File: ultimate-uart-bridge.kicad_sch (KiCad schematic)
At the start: 22 parts, among them J101 Conn_02x03_Row_Letter_First

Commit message: New inital routing
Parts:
- C101, C102: value (none) -> 1uF; footprint (none) -> Capacitor_SMD:C_0805_2012Metric_Pad1.18x1.45mm_HandSolder
- C103, C104: value (none) -> 47pF; footprint (none) -> Capacitor_SMD:C_0805_2012Metric_Pad1.18x1.45mm_HandSolder
- C105, C107: value (none) -> 100nF; footprint (none) -> Capacitor_SMD:C_0805_2012Metric_Pad1.18x1.45mm_HandSolder
- C106: value (none) -> 10nF; footprint (none) -> Capacitor_SMD:C_0805_2012Metric_Pad1.18x1.45mm_HandSolder
- C108: value (none) -> 4.7uF; footprint (none) -> Capacitor_SMD:C_0805_2012Metric_Pad1.18x1.45mm_HandSolder
- D101, D102: value (none) -> LED; footprint (none) -> LED_SMD:LED_0805_2012Metric_Pad1.15x1.40mm_HandSolder
- FB101: value (none) -> Ferrite_Bead_Small; footprint (none) -> Inductor_SMD:L_0805_2012Metric_Pad1.15x1.40mm_HandSolder
- I101: value (none) -> MIC5317-1.8YM5-TR
- I102: value (none) -> FT231XS; footprint (none) -> Package_SO:SSOP-20_3.9x8.7mm_P0.635mm
- J101: footprint (none) -> Connector_PinHeader_2.54mm:PinHeader_2x03_P2.54mm_Vertical_SMD; symbol Connector_Generic:Conn_02x03_Row_Letter_First -> Connector_Generic:Conn_02x03_Odd_Even
- J102: value (none) -> USB_C_Receptacle_USB2.0; footprint (none) -> Connector_USB:USB_C_Receptacle_GCT_USB4085
- J103: value (none) -> Conn_01x03; footprint (none) -> Connector_PinHeader_2.54mm:PinHeader_1x03_P2.54mm_Vertical_SMD_Pin1Left
- R101, R102: value (none) -> 27; footprint (none) -> Resistor_SMD:R_0805_2012Metric_Pad1.20x1.40mm_HandSolder
- R103, R104: value (none) -> R; footprint (none) -> Resistor_SMD:R_0805_2012Metric_Pad1.20x1.40mm_HandSolder
- R105, R106: value (none) -> 5.1k; footprint (none) -> Resistor_SMD:R_0805_2012Metric_Pad1.20x1.40mm_HandSolder
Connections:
- net +1V8: now also J101.6 (Pin_6); no longer J101.b3 (Pin_b3)
- net +3V3: now also J101.4 (Pin_4); no longer J101.b2 (Pin_b2)
- net VBUS: now also J101.2 (Pin_2); no longer J101.b1 (Pin_b1)
- net VCCIO: now also J101.1 (Pin_1), J101.3 (Pin_3), J101.5 (Pin_5); no longer J101.a1 (Pin_a1), J101.a2 (Pin_a2), J101.a3 (Pin_a3)

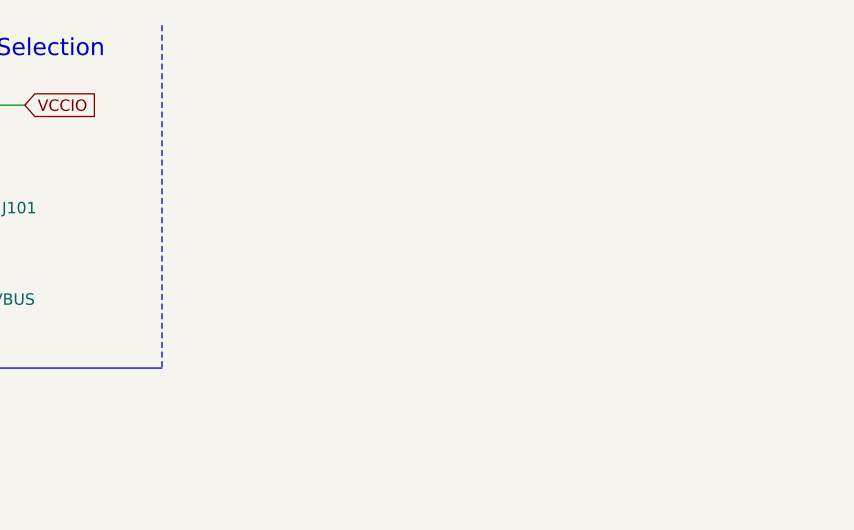
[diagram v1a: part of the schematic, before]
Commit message: Add testpoints and text
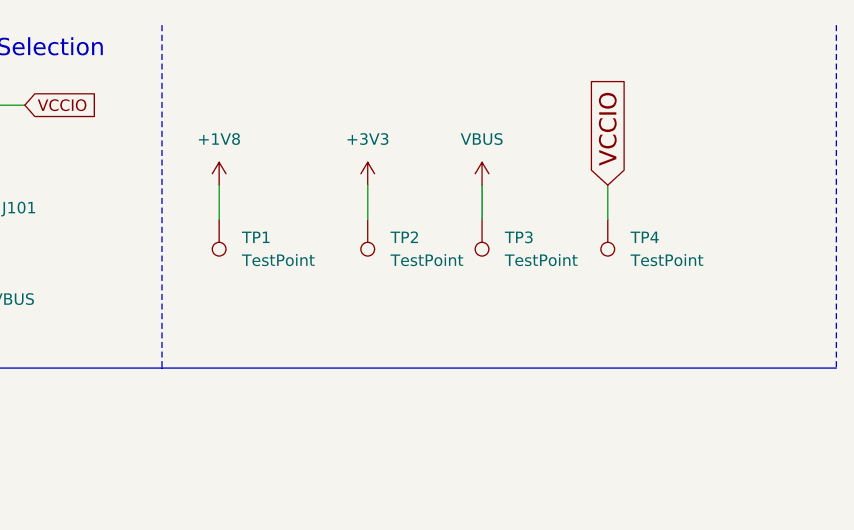
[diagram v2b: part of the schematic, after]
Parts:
- added TP1, TP2, TP3, TP4: TestPoint, TestPoint:TestPoint_Pad_D3.0mm, symbol Connector:TestPoint
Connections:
- net +1V8: now also TP1.1
- net +3V3: now also TP2.1
- net VBUS: now also TP3.1
- net VCCIO: now also TP4.1
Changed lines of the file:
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@@
+    (stroke (width 0) (type default) (color 0 0 0 0))
+  )
+  (wire (pts (xy 179.07 30.48) (xy 179.07 34.29))
     (stroke (width 0) (type default) (color 0 0 0 0))
   )
@@
     (stroke (width 0) (type default) (color 0 0 0 0))
   )
+  (wire (pts (xy 208.28 30.48) (xy 208.28 34.29))
+    (stroke (width 0) (type default) (color 0 0 0 0))
+  )
   (wire (pts (xy 109.22 90.17) (xy 119.38 90.17))
     (stroke (width 0) (type default) (color 0 0 0 0))
@@
   )
   (wire (pts (xy 54.61 83.82) (xy 50.8 83.82))
+    (stroke (width 0) (type default) (color 0 0 0 0))
+  )
+  (wire (pts (xy 222.25 30.48) (xy 222.25 34.29))
     (stroke (width 0) (type default) (color 0 0 0 0))
   )
@@
     (stroke (width 0) (type default) (color 0 0 0 0))
   )
+  (polyline (pts (xy 172.72 50.8) (xy 247.65 50.8))
+    (stroke (width 0) (type default) (color 0 0 0 1))
+  )
   (wire (pts (xy 34.29 29.21) (xy 41.91 29.21))
+    (stroke (width 0) (type default) (color 0 0 0 0))
+  )
+  (wire (pts (xy 195.58 30.48) (xy 195.58 34.29))
     (stroke (width 0) (type default) (color 0 0 0 0))
   )
@@
   (wire (pts (xy 50.8 81.28) (xy 54.61 81.28))
     (stroke (width 0) (type default) (color 0 0 0 0))
+  )
+  (polyline (pts (xy 247.65 12.7) (xy 247.65 50.8))
+    (stroke (width 0) (type dash) (color 0 0 0 1))
   )
   (wire (pts (xy 54.61 81.28) (xy 54.61 83.82))
@@
     (property "Intersheet References" "${INTERSHEET_REFS}" (id 0) (at 0 0 0)
       (effects (font (size 1.27 1.27)) hide)
+    )
+  )
+  (global_label "VCCIO" (shape input) (at 222.25 30.48 90) (fields_autoplaced)
+    (effects (font (size 1.905 1.905)) (justify left))
+    (property "Intersheet References" "${INTERSHEET_REFS}" (id 0) (at 222.131 18.6482 90)
+      (effects (font (size 1.905 1.905)) (justify left) hide)
     )
   )
@@
     (pin "1")
   )
+  (symbol (lib_id "Connector:TestPoint") (at 195.58 34.29 180) (unit 1)
+    (in_bom yes) (on_board yes) (fields_autoplaced)
+    (property "Reference" "TP2" (id 0) (at 198.12 36.3219 0)
+      (effects (font (size 1.27 1.27)) (justify right))
+    )
+    (property "Value" "TestPoint" (id 1) (at 198.12 38.8619 0)
+      (effects (font (size 1.27 1.27)) (justify right))
+    )
+    (property "Footprint" "TestPoint:TestPoint_Pad_D3.0mm" (id 2) (at 190.5 34.29 0)
+      (effects (font (size 1.27 1.27)) hide)
+    )
+    (property "Datasheet" "~" (id 3) (at 190.5 34.29 0)
+      (effects (font (size 1.27 1.27)) hide)
+    )
+    (pin "1")
+  )
+  (symbol (lib_id "power:VBUS") (at 208.28 30.48 0) (unit 1)
+    (in_bom yes) (on_board yes) (fields_autoplaced)
+    (property "Reference" "#PWR03" (id 0) (at 208.28 34.29 0)
+      (effects (font (size 1.27 1.27)) hide)
+    )
+    (property "Value" "VBUS" (id 1) (at 208.28 25.4 0))
+    (property "Footprint" "" (id 2) (at 208.28 30.48 0)
+      (effects (font (size 1.27 1.27)) hide)
+    )
+    (property "Datasheet" "" (id 3) (at 208.28 30.48 0)
+      (effects (font (size 1.27 1.27)) hide)
+    )
+    (pin "1")
+  )
+  (symbol (lib_id "Connector:TestPoint") (at 208.28 34.29 180) (unit 1)
+    (in_bom yes) (on_board yes) (fields_autoplaced)
+    (property "Reference" "TP3" (id 0) (at 210.82 36.3219 0)
+      (effects (font (size 1.27 1.27)) (justify right))
+    )
+    (property "Value" "TestPoint" (id 1) (at 210.82 38.8619 0)
+      (effects (font (size 1.27 1.27)) (justify right))
+    )
+    (property "Footprint" "TestPoint:TestPoint_Pad_D3.0mm" (id 2) (at 203.2 34.29 0)
+      (effects (font (size 1.27 1.27)) hide)
+    )
+    (property "Datasheet" "~" (id 3) (at 203.2 34.29 0)
+      (effects (font (size 1.27 1.27)) hide)
+    )
+    (pin "1")
+  )
+  (symbol (lib_id "power:+3V3") (at 195.58 30.48 0) (unit 1)
+    (in_bom yes) (on_board yes) (fields_autoplaced)
+    (property "Reference" "#PWR02" (id 0) (at 195.58 34.29 0)
+      (effects (font (size 1.27 1.27)) hide)
+    )
+    (property "Value" "+3V3" (id 1) (at 195.58 25.4 0))
+    (property "Footprint" "" (id 2) (at 195.58 30.48 0)
+      (effects (font (size 1.27 1.27)) hide)
+    )
+    (property "Datasheet" "" (id 3) (at 195.58 30.48 0)
+      (effects (font (size 1.27 1.27)) hide)
+    )
+    (pin "1")
+  )
+  (symbol (lib_id "Connector:TestPoint") (at 179.07 34.29 180) (unit 1)
+    (in_bom yes) (on_board yes) (fields_autoplaced)
+    (property "Reference" "TP1" (id 0) (at 181.61 36.3219 0)
+      (effects (font (size 1.27 1.27)) (justify right))
+    )
+    (property "Value" "TestPoint" (id 1) (at 181.61 38.8619 0)
+      (effects (font (size 1.27 1.27)) (justify right))
+    )
+    (property "Footprint" "TestPoint:TestPoint_Pad_D3.0mm" (id 2) (at 173.99 34.29 0)
+      (effects (font (size 1.27 1.27)) hide)
+    )
+    (property "Datasheet" "~" (id 3) (at 173.99 34.29 0)
+      (effects (font (size 1.27 1.27)) hide)
+    )
+    (pin "1")
+  )
+  (symbol (lib_id "Connector:TestPoint") (at 222.25 34.29 180) (unit 1)
+    (in_bom yes) (on_board yes) (fields_autoplaced)
+    (property "Reference" "TP4" (id 0) (at 224.79 36.3219 0)
+      (effects (font (size 1.27 1.27)) (justify right))
+    )
+    (property "Value" "TestPoint" (id 1) (at 224.79 38.8619 0)
+      (effects (font (size 1.27 1.27)) (justify right))
+    )
+    (property "Footprint" "TestPoint:TestPoint_Pad_D3.0mm" (id 2) (at 217.17 34.29 0)
+      (effects (font (size 1.27 1.27)) hide)
+    )
+    (property "Datasheet" "~" (id 3) (at 217.17 34.29 0)
+      (effects (font (size 1.27 1.27)) hide)
+    )
+    (pin "1")
+  )
+  (symbol (lib_id "power:+1V8") (at 179.07 30.48 0) (unit 1)
+    (in_bom yes) (on_board yes) (fields_autoplaced)
+    (property "Reference" "#PWR01" (id 0) (at 179.07 34.29 0)
+      (effects (font (size 1.27 1.27)) hide)
+    )
+    (property "Value" "+1V8" (id 1) (at 179.07 25.4 0))
+    (property "Footprint" "" (id 2) (at 179.07 30.48 0)
+      (effects (font (size 1.27 1.27)) hide)
+    )
+    (property "Datasheet" "" (id 3) (at 179.07 30.48 0)
+      (effects (font (size 1.27 1.27)) hide)
+    )
+    (pin "1")
+  )
   (sheet_instances
     (path "/" (page "1"))
   )
   (symbol_instances
+    (path "/d447cd8d-505f-45cd-b508-7b48bbd46143"
+      (reference "#PWR01") (unit 1) (value "+1V8") (footprint "")
+    )
+    (path "/918c1faf-a3b6-4f0c-9710-820ea771bcfb"
+      (reference "#PWR02") (unit 1) (value "+3V3") (footprint "")
+    )
+    (path "/51ff3703-38a9-4abd-b6b0-2e764a7ec977"
+      (reference "#PWR03") (unit 1) (value "VBUS") (footprint "")
+    )
     (path "/00000000-0000-0000-0000-000060fe5cbe"
       (reference "#PWR0101") (unit 1) (value "VBUS") (footprint "")
@@
       (reference "R106") (unit 1) (value "5.1k") (footprint "Resistor_SMD:R_0805_2012Metric_Pad1.20x1.40mm_HandSolder")
     )
-  )
+    (path "/b6ba5c02-0398-48b3-9194-4c168c5cb2de"
+      (reference "TP1") (unit 1) (value "TestPoint") (footprint "TestPoint:TestPoint_Pad_D3.0mm")
+    )
+    (path "/1011f139-ec9e-4d31-a10a-d23eea101c42"
+      (reference "TP2") (unit 1) (value "TestPoint") (footprint "TestPoint:TestPoint_Pad_D3.0mm")
+    )
+    (path "/6f46363d-2716-45e5-a546-b6a0dc7e617b"
+      (reference "TP3") (unit 1) (value "TestPoint") (footprint "TestPoint:TestPoint_Pad_D3.0mm")
+    )
+    (path "/c1648b49-bfbb-4859-b4f7-86ccb46b94c0"
+      (reference "TP4") (unit 1) (value "TestPoint") (footprint "TestPoint:TestPoint_Pad_D3.0mm")
+    )
+  )

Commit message: New stuff
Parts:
- C101, C102: JLC (none) -> C28323; PartNo (none) -> CL21B105KBFNNNE
- C103, C104: JLC (none) -> C14857; PartNo (none) -> CL21C470JBANNNC
- C105, C107: JLC (none) -> C49678; PartNo (none) -> CC0805KRX7R9BB104
- C106: JLC (none) -> C1710; PartNo (none) -> CL21B103KBANNNC
- C108: JLC (none) -> C1779; PartNo (none) -> CL21A475KAQNNNE
- D101, D102: JLC (none) -> C84256; PartNo (none) -> NCD0805R1
- I101: PartNo (none) -> MIC5317-1.8YM5
- I102: JLC (none) -> C132160; PartNo (none) -> FT231XS
- J101: PartNo (none) -> TSM-103-02-T-DV
- J102: PartNo (none) -> USB4085-GF-A
- J103: PartNo (none) -> TSM-103-02-T-SV
- R101, R102: JLC (none) -> C17594; PartNo (none) -> 0805W8F270JT5E
- R103, R104: value R -> 120; JLC (none) -> C17437; PartNo (none) -> 0805W8F1200T5E
- R105, R106: JLC (none) -> C27834; PartNo (none) -> 0805W8F5101T5E
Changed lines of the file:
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@@
+      (effects (font (size 1.27 1.27)) hide)
+    )
+    (property "JLC" "C132160" (id 4) (at 137.16 95.25 0)
+      (effects (font (size 1.27 1.27)) hide)
+    )
+    (property "PartNo" "FT231XS" (id 5) (at 137.16 95.25 0)
       (effects (font (size 1.27 1.27)) hide)
     )
@@
       (effects (font (size 1.524 1.524)) hide)
     )
+    (property "PartNo" "MIC5317-1.8YM5" (id 4) (at 53.34 29.21 0)
+      (effects (font (size 1.27 1.27)) hide)
+    )
     (pin "1")
     (pin "2")
@@
       (effects (font (size 1.27 1.27)) hide)
     )
+    (property "JLC" "C28323" (id 4) (at 34.29 33.02 0)
+      (effects (font (size 1.27 1.27)) hide)
+    )
+    (property "PartNo" "CL21B105KBFNNNE" (id 5) (at 34.29 33.02 0)
+      (effects (font (size 1.27 1.27)) hide)
+    )
     (pin "1")
     (pin "2")
@@
     )
     (property "Datasheet" "~" (id 3) (at 114.3 35.56 0)
+      (effects (font (size 1.27 1.27)) hide)
+    )
+    (property "JLC" "C28323" (id 4) (at 114.3 35.56 0)
+      (effects (font (size 1.27 1.27)) hide)
+    )
+    (property "PartNo" "CL21B105KBFNNNE" (id 5) (at 114.3 35.56 0)
       (effects (font (size 1.27 1.27)) hide)
     )
@@
       (effects (font (size 1.27 1.27)) hide)
     )
+    (property "JLC" "C49678" (id 4) (at 116.84 76.2 0)
+      (effects (font (size 1.27 1.27)) hide)
+    )
+    (property "PartNo" "CC0805KRX7R9BB104" (id 5) (at 116.84 76.2 0)
+      (effects (font (size 1.27 1.27)) hide)
+    )
     (pin "1")
     (pin "2")
@@
       (effects (font (size 1.27 1.27)) hide)
     )
+    (property "JLC" "C14857" (id 4) (at 59.69 105.41 0)
+      (effects (font (size 1.27 1.27)) hide)
+    )
+    (property "PartNo" "CL21C470JBANNNC" (id 5) (at 59.69 105.41 0)
+      (effects (font (size 1.27 1.27)) hide)
+    )
     (pin "1")
     (pin "2")
@@
     )
     (property "Datasheet" "~" (id 3) (at 66.04 105.41 0)
+      (effects (font (size 1.27 1.27)) hide)
+    )
+    (property "JLC" "C14857" (id 4) (at 66.04 105.41 0)
+      (effects (font (size 1.27 1.27)) hide)
+    )
+    (property "PartNo" "CL21C470JBANNNC" (id 5) (at 66.04 105.41 0)
       (effects (font (size 1.27 1.27)) hide)
     )
@@
       (effects (font (size 1.27 1.27)) hide)
     )
+    (property "JLC" "C17594" (id 4) (at 72.39 88.9 0)
+      (effects (font (size 1.27 1.27)) hide)
+    )
+    (property "PartNo" "0805W8F270JT5E" (id 5) (at 72.39 88.9 0)
+      (effects (font (size 1.27 1.27)) hide)
+    )
     (pin "1")
     (pin "2")
@@
       (effects (font (size 1.27 1.27)) hide)
     )
+    (property "JLC" "C17594" (id 4) (at 72.39 81.28 0)
+      (effects (font (size 1.27 1.27)) hide)
+    )
+    (property "PartNo" "0805W8F270JT5E" (id 5) (at 72.39 81.28 0)
+      (effects (font (size 1.27 1.27)) hide)
+    )
     (pin "1")
     (pin "2")
@@
       (effects (font (size 1.27 1.27)) hide)
     )
+    (property "JLC" "C1710" (id 4) (at 50.8 130.81 0)
+      (effects (font (size 1.27 1.27)) hide)
+    )
+    (property "PartNo" "CL21B103KBANNNC" (id 5) (at 50.8 130.81 0)
+      (effects (font (size 1.27 1.27)) hide)
+    )
     (pin "1")
     (pin "2")
@@
       (effects (font (size 1.27 1.27)) hide)
     )
+    (property "JLC" "C49678" (id 4) (at 60.96 130.81 0)
+      (effects (font (size 1.27 1.27)) hide)
+    )
+    (property "PartNo" "CC0805KRX7R9BB104" (id 5) (at 60.96 130.81 0)
+      (effects (font (size 1.27 1.27)) hide)
+    )
     (pin "1")
     (pin "2")
@@
       (effects (font (size 1.27 1.27)) hide)
     )
+    (property "JLC" "C1779" (id 4) (at 72.39 130.81 0)
+      (effects (font (size 1.27 1.27)) hide)
+    )
+    (property "PartNo" "CL21A475KAQNNNE" (id 5) (at 72.39 130.81 0)
+      (effects (font (size 1.27 1.27)) hide)
+    )
     (pin "1")
     (pin "2")
@@
       (effects (font (size 1.27 1.27)) (justify left))
     )
-    (property "Value" "R" (id 1) (at 173.228 102.743 0)
+    (property "Value" "120" (id 1) (at 173.228 102.743 0)
       (effects (font (size 1.27 1.27)) (justify left))
     )
@@
       (effects (font (size 1.27 1.27)) hide)
     )
+    (property "PartNo" "0805W8F1200T5E" (id 4) (at 171.45 101.6 0)
+      (effects (font (size 1.27 1.27)) hide)
+    )
+    (property "JLC" "C17437" (id 5) (at 171.45 101.6 0)
+      (effects (font (size 1.27 1.27)) hide)
+    )
     (pin "1")
     (pin "2")
@@
       (effects (font (size 1.27 1.27)) hide)
     )
+    (property "JLC" "C84256" (id 4) (at 171.45 91.44 0)
+      (effects (font (size 1.27 1.27)) hide)
+    )
+    (property "PartNo" "NCD0805R1" (id 5) (at 171.45 91.44 0)
+      (effects (font (size 1.27 1.27)) hide)
+    )
     (pin "1")
     (pin "2")
@@
       (effects (font (size 1.27 1.27)) (justify left))
     )
-    (property "Value" "R" (id 1) (at 184.658 102.743 0)
+    (property "Value" "120" (id 1) (at 184.658 102.743 0)
       (effects (font (size 1.27 1.27)) (justify left))
     )
@@
       (effects (font (size 1.27 1.27)) hide)
     )
+    (property "PartNo" "0805W8F1200T5E" (id 4) (at 182.88 101.6 0)
+      (effects (font (size 1.27 1.27)) hide)
+    )
+    (property "JLC" "C17437" (id 5) (at 182.88 101.6 0)
+      (effects (font (size 1.27 1.27)) hide)
+    )
     (pin "1")
     (pin "2")
@@
       (effects (font (size 1.27 1.27)) hide)
     )
+    (property "JLC" "C84256" (id 4) (at 182.88 91.44 0)
+      (effects (font (size 1.27 1.27)) hide)
+    )
+    (property "PartNo" "NCD0805R1" (id 5) (at 182.88 91.44 0)
+      (effects (font (size 1.27 1.27)) hide)
+    )
     (pin "1")
     (pin "2")
@@
     )
     (property "Datasheet" "~" (id 3) (at 208.28 78.74 0)
+      (effects (font (size 1.27 1.27)) hide)
+    )
+    (property "PartNo" "TSM-103-02-T-SV" (id 4) (at 208.28 78.74 0)
       (effects (font (size 1.27 1.27)) hide)
     )
@@
     )
     (property "Datasheet" "~" (id 3) (at 149.86 31.75 0)
+      (effects (font (size 1.27 1.27)) hide)
+    )
+    (property "PartNo" "TSM-103-02-T-DV" (id 4) (at 149.86 31.75 0)
       (effects (font (size 1.27 1.27)) hide)
     )
@@
     )
     (property "Datasheet" "https://www.usb.org/sites/default/files/documents/usb_type-c.zip" (id 3) (at 39.37 83.82 0)
+      (effects (font (size 1.27 1.27)) hide)
+    )
+    (property "PartNo" "USB4085-GF-A" (id 4) (at 35.56 83.82 0)
       (effects (font (size 1.27 1.27)) hide)
     )
@@
       (effects (font (size 1.27 1.27)) hide)
     )
+    (property "JLC" "C27834" (id 4) (at 55.88 73.66 0)
+      (effects (font (size 1.27 1.27)) hide)
+    )
+    (property "PartNo" "0805W8F5101T5E" (id 5) (at 55.88 73.66 0)
+      (effects (font (size 1.27 1.27)) hide)
+    )
     (pin "1")
     (pin "2")
@@
       (effects (font (size 1.27 1.27)) hide)
     )
+    (property "JLC" "C27834" (id 4) (at 55.88 76.2 0)
+      (effects (font (size 1.27 1.27)) hide)
+    )
+    (property "PartNo" "0805W8F5101T5E" (id 5) (at 55.88 76.2 0)
+      (effects (font (size 1.27 1.27)) hide)
+    )
     (pin "1")
     (pin "2")
@@
     )
     (path "/00000000-0000-0000-0000-000061012f4a"
-      (reference "R103") (unit 1) (value "R") (footprint "Resistor_SMD:R_0805_2012Metric_Pad1.20x1.40mm_HandSolder")
+      (reference "R103") (unit 1) (value "120") (footprint "Resistor_SMD:R_0805_2012Metric_Pad1.20x1.40mm_HandSolder")
     )
     (path "/00000000-0000-0000-0000-0000610163e6"
-      (reference "R104") (unit 1) (value "R") (footprint "Resistor_SMD:R_0805_2012Metric_Pad1.20x1.40mm_HandSolder")
+      (reference "R104") (unit 1) (value "120") (footprint "Resistor_SMD:R_0805_2012Metric_Pad1.20x1.40mm_HandSolder")
     )
     (path "/00000000-0000-0000-0000-00006223e8fa"
